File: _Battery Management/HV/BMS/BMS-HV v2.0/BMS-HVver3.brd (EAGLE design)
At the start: 152.4 x 124.8 mm, 428 parts, among them J3 M2S02B-PASK-2(LF)(SN), J4 M2S02B-PASK-2(LF)(SN), Q1 BSS308PE, Q10 BSS308PE, Q11 BSS308PE, Q12 BSS308PE, Q13 BSS308PE, Q14 BSS308PE, Q15 BSS308PE, Q16 BSS308PE, Q17 BSS308PE, Q18 BSS308PE, Q19 BSS308PE, Q2 BSS308PE, Q20 BSS308PE, Q21 BSS308PE, Q22 BSS308PE, Q23 BSS308PE, Q24 BSS308PE, Q25 BSS308PE, Q26 BSS308PE, Q27 BSS308PE, Q28 BSS308PE, Q29 BSS308PE, Q3 BSS308PE, Q30 BSS308PE, Q31 BSS308PE, Q32 BSS308PE, Q33 BSS308PE, Q34 BSS308PE, Q35 BSS308PE, Q36 BSS308PE, Q37 BSS308PE, Q38 BSS308PE, Q39 BSS308PE, Q4 BSS308PE, Q5 BSS308PE, Q6 BSS308PE, Q7 BSS308PE, Q8 BSS308PE, Q9 BSS308PE, U1 LTC6804-2, U2 LTC6804-2, U3 LTC6804-2

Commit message: BMS Redo
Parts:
- removed R54, R55, R56, R57, R58, R59, R60, R61, R62, R63, R64, R65: 16, FSAE Electric:RR02J16RTB
- R42, R43, R44, R45, R46, R47, R48, R49, R50, R51, R52, R53: value 16 -> (none); device FSAE Electric:RR02J16RTB -> adafruit:R2512
- moved R42 95.5 mm to (102.3, 31.2), turned to 0 degrees
- moved R43 86.8 mm to (102.3, 25.6)
- moved R44 84.6 mm to (102.3, 20.0), turned to 0 degrees
- moved R45 76.8 mm to (102.3, 14.4)
- moved R46 76.4 mm to (102.3, 8.79), turned to 0 degrees
- moved R52 74.4 mm to (102.3, -24.9), turned to 0 degrees
- moved R53 74.2 mm to (102.3, -30.5)
- moved R48 71.5 mm to (102.3, -2.44), turned to 0 degrees
- moved R50 70.8 mm to (102.3, -13.7), turned to 0 degrees
- moved R47 69.8 mm to (102.3, 3.17)
- moved R51 68.4 mm to (102.3, -19.3)
- moved R49 66.8 mm to (102.3, -8.05)
- moved D24 20.6 mm to (-22.0, -46.1), turned to 270 degrees
- moved D23 19.6 mm to (-22.1, -38.6), turned to 270 degrees
- moved D22 18.9 mm to (-22.1, -31.1), turned to 270 degrees
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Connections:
- net N$10: now also R44.2; no longer R60.P$2, R61.P$2
- net N$12: now also R44.1; no longer R60.P$1, R61.P$1
- net N$14: now also R45.2; no longer R58.P$2, R59.P$2
- net N$16: now also R45.1; no longer R58.P$1, R59.P$1
- net N$18: now also R46.2; no longer R56.P$2, R57.P$2
- net N$2: now also R42.2; no longer R64.P$2, R65.P$2
- net N$21: now also R48.2; no longer R52.P$2, R53.P$2
- net N$23: now also R46.1; no longer R56.P$1, R57.P$1
- net N$25: now also R47.2; no longer R54.P$2, R55.P$2
- net N$27: now also R47.1; no longer R54.P$1, R55.P$1
- net N$28: now also R48.1; no longer R52.P$1, R53.P$1
- net N$30: now also R49.2; no longer R50.P$2, R51.P$2
- net N$32: now also R49.1; no longer R50.P$1, R51.P$1
- net N$34: now also R50.2; no longer R48.P$2, R49.P$2
- net N$36: now also R50.1; no longer R48.P$1, R49.P$1
- net N$38: now also R51.2; no longer R46.P$2, R47.P$2
- net N$4: now also R42.1; no longer R64.P$1, R65.P$1
- net N$40: now also R51.1; no longer R46.P$1, R47.P$1
- net N$42: now also R52.2; no longer R44.P$2, R45.P$2
- net N$47: now also R53.2; no longer R42.P$2, R43.P$2
- net N$48: now also R53.1; no longer R42.P$1, R43.P$1
- net N$49: now also R52.1; no longer R44.P$1, R45.P$1
- net N$6: now also R43.2; no longer R62.P$2, R63.P$2
- net N$8: now also R43.1; no longer R62.P$1, R63.P$1
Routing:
- net GPIO1: track 69.8 -> 0.00 mm, vias 2 -> 0
- net GPIO2: track 61.6 -> 0.00 mm, vias 3 -> 0
- net IMA2: track 165.6 -> 105.1 mm, vias 2 -> 1
- net IPA2: track 156.5 -> 97.2 mm, vias 2 -> 1
- net IPA: track 105.3 -> 52.5 mm, vias 4 -> 3
- net IMA: track 121.9 -> 69.8 mm, vias 4 -> 3
- net N$170: track 53.3 -> 3.50 mm
- net C0: track 108.9 -> 61.3 mm, vias 1 -> 0
- net VREF2: track 40.8 -> 0.00 mm, vias 3 -> 0
- net GPIO4: track 39.9 -> 0.00 mm, vias 2 -> 0
- net VREG: track 36.8 -> 1.74 mm, vias 1 -> 0
- net GPIO3: track 31.7 -> 0.00 mm, vias 2 -> 0
- net DRIVE: track 28.8 -> 0.00 mm
- net N$103: track 3.15 -> 27.5 mm
- net A0: track 20.7 -> 0.00 mm, vias 2 -> 0
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
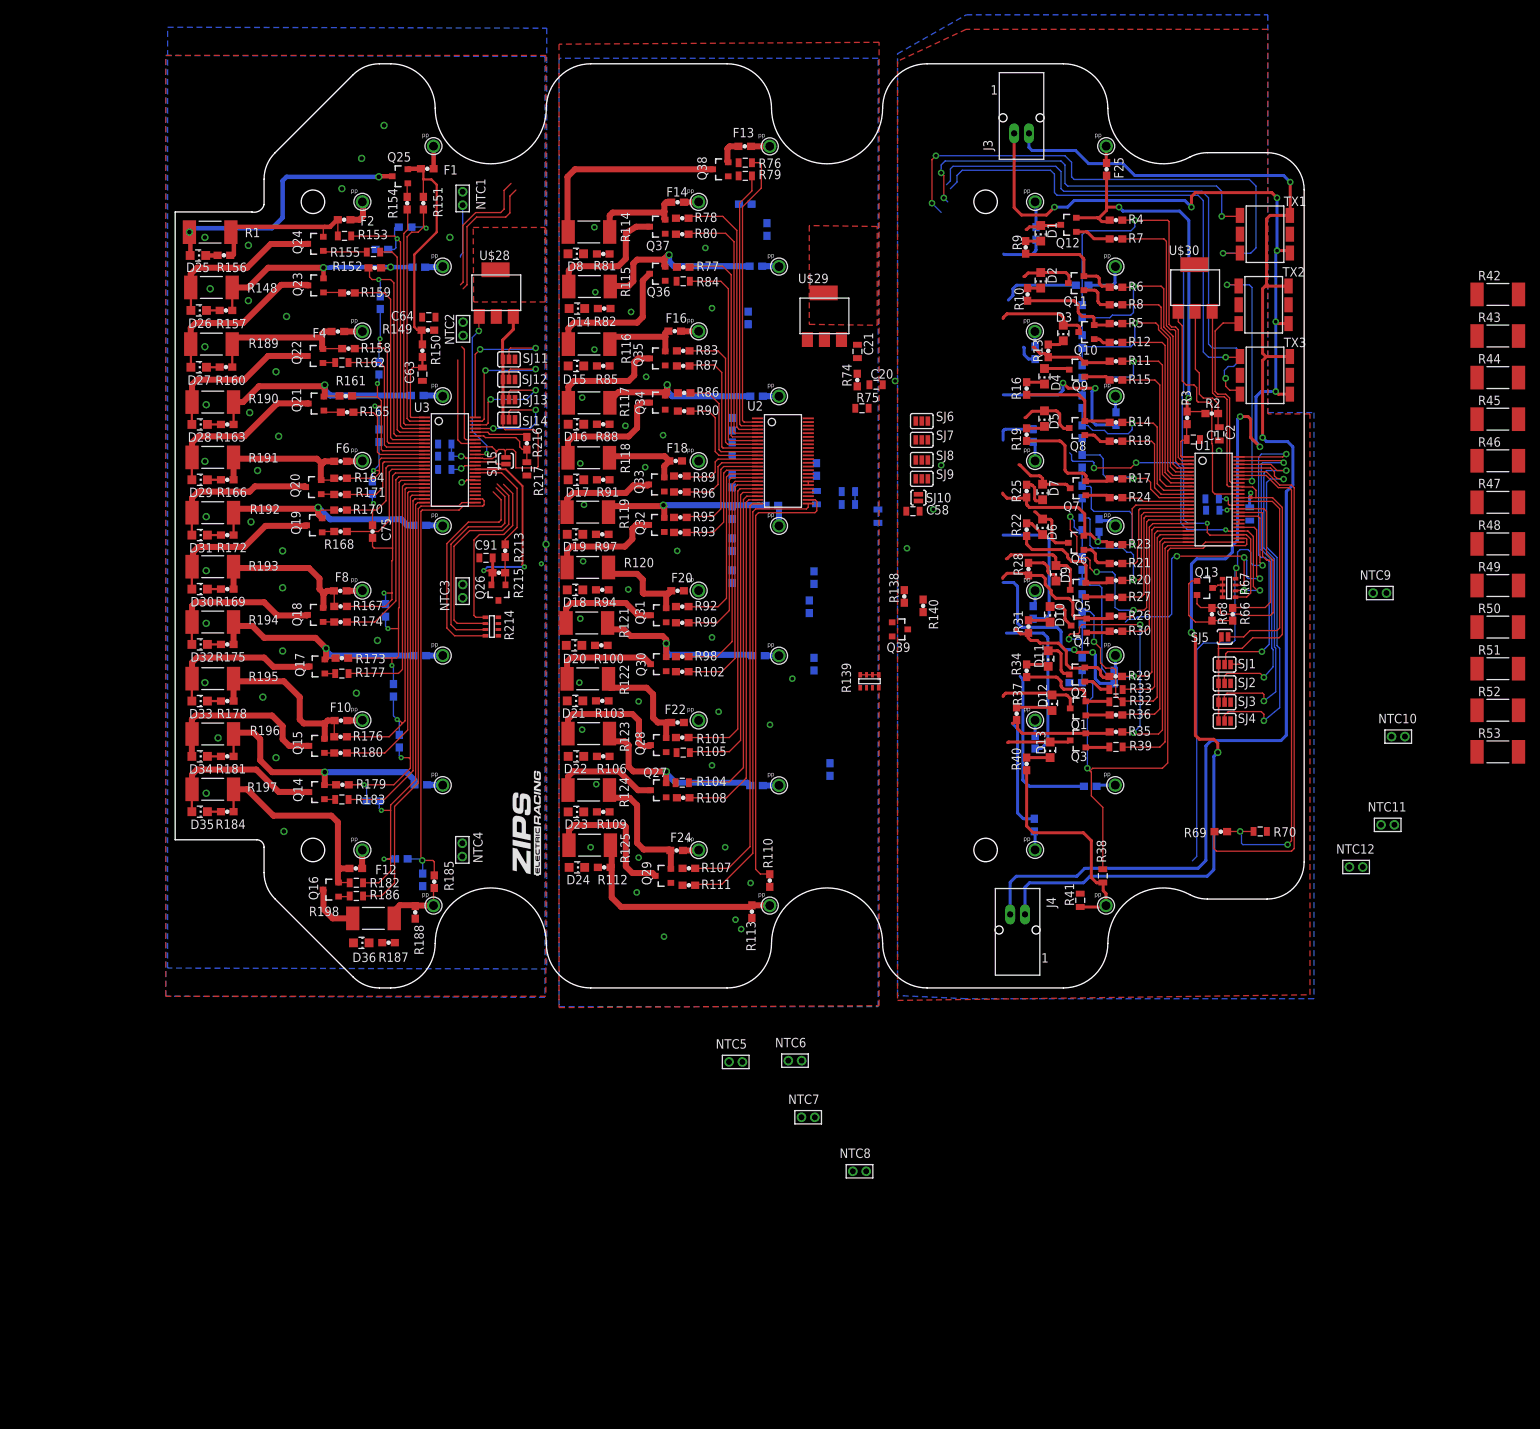
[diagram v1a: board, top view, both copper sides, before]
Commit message: 
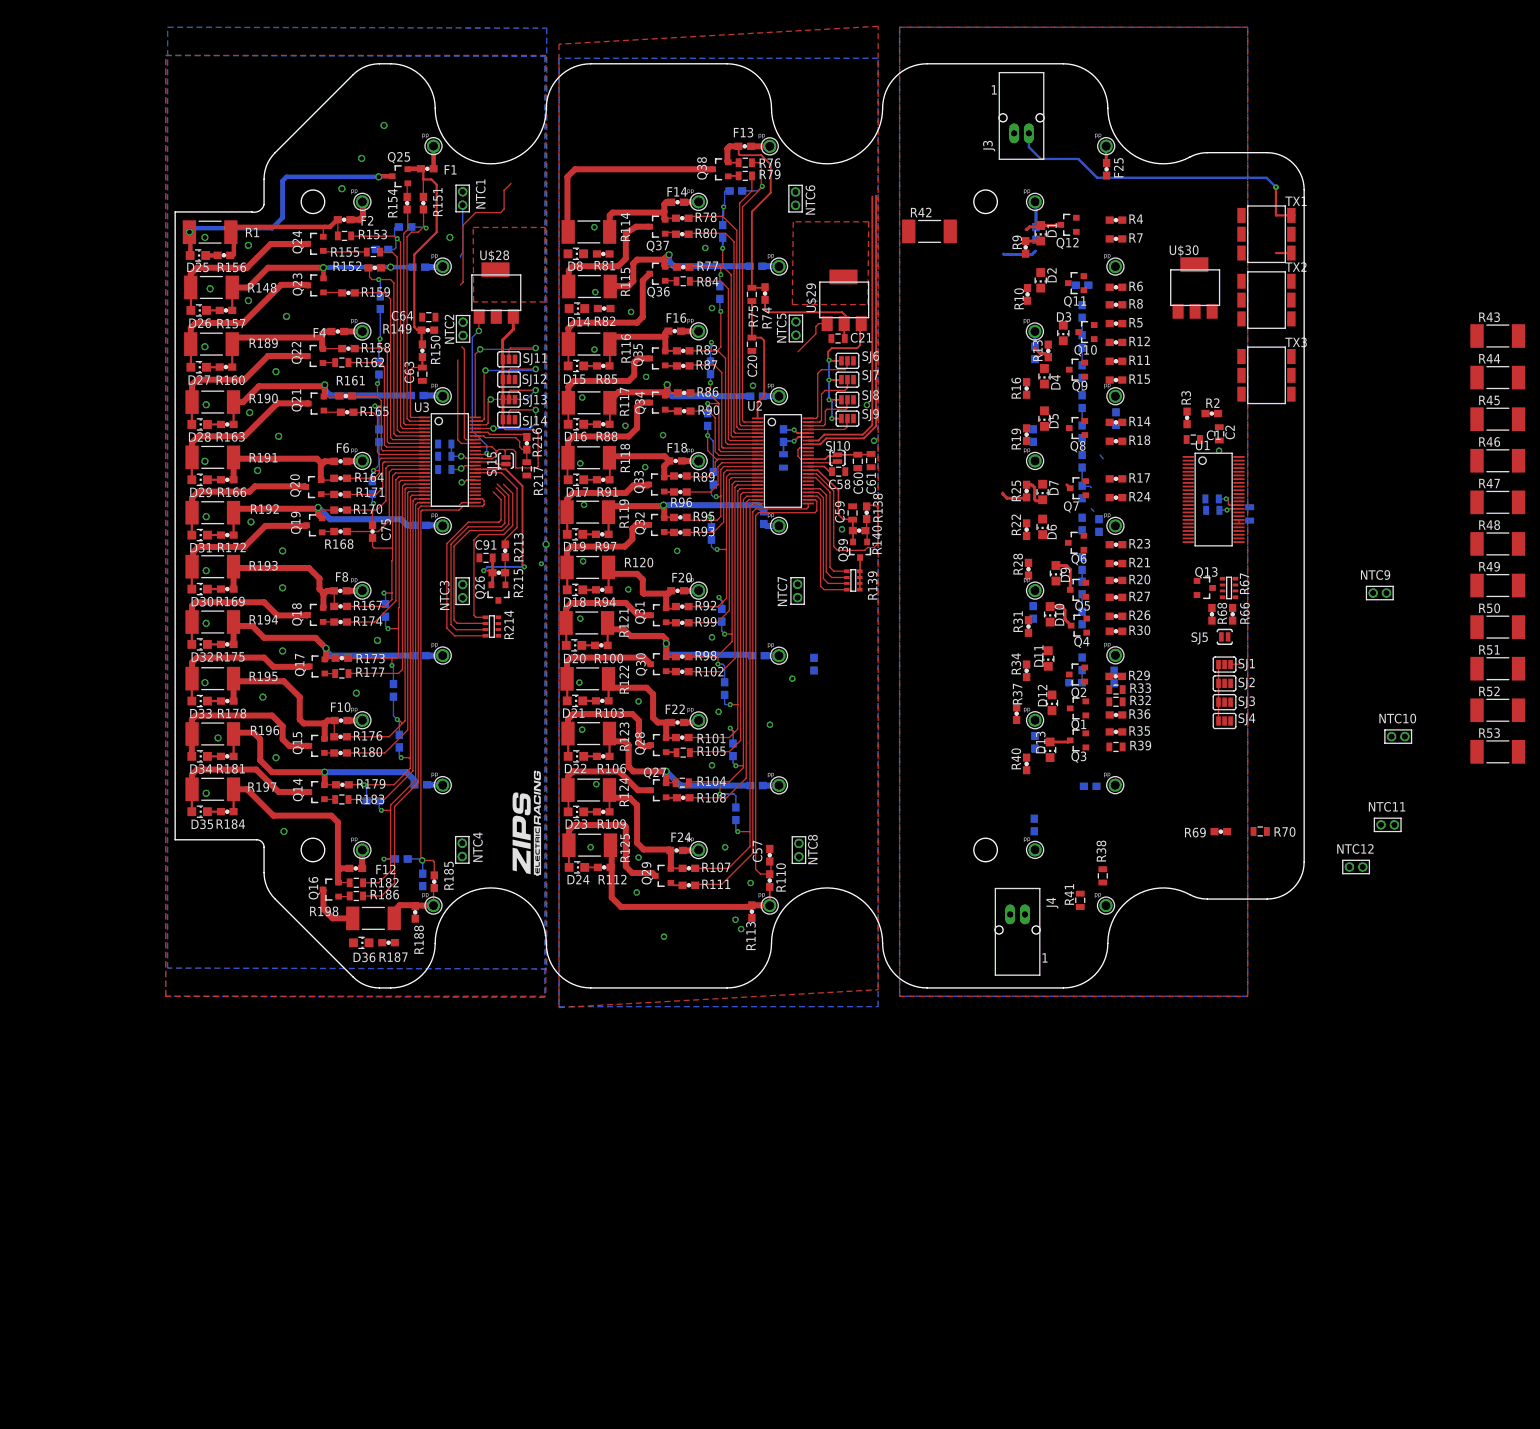
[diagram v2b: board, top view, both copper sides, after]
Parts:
- moved NTC6 116.4 mm to (7.54, 44.2), turned to 90 degrees
- moved NTC5 99.3 mm to (7.59, 26.6), turned to 90 degrees
- moved R42 77.2 mm to (25.6, 39.8)
- moved NTC7 71.1 mm to (7.82, -8.79), turned to 90 degrees
- moved NTC8 44.1 mm to (8.00, -43.8), turned to 90 degrees
- moved C53 29.6 mm to (-0.51, -38.9)
- moved C51 25.7 mm to (-0.89, -30.2)
- moved R75 21.4 mm to (1.65, 31.2), turned to 270 degrees
- moved C20 17.6 mm to (1.65, 24.5), turned to 270 degrees
- moved R74 17.1 mm to (3.43, 31.4), turned to 270 degrees
- moved C49 15.1 mm to (-2.03, -22.0)
- moved C57 14.1 mm to (4.06, -44.5), flipped to the top, turned to 90 degrees
- moved R139 13.8 mm to (15.4, -7.37), turned to 270 degrees
- moved R140 13.3 mm to (16.1, -0.64), turned to 180 degrees
- moved SJ6 12.9 mm to (14.6, 22.3)
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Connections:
- new net N$109: NTC8.2
- net GNDA: no longer NTC8.1
- net GPIO1: now also R139.4; no longer NTC5.2, R139.1
- net GPIO2: now also R139.3; no longer NTC6.2, R139.2
- net GPIO3: now also R139.2; no longer NTC7.2, R139.3
- net GPIO4: now also R139.1; no longer NTC8.2, R139.4
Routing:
- net N$129: track 195.9 -> 2.08 mm, vias 10 -> 0
- net N$125: track 186.3 -> 43.8 mm, vias 2 -> 1
- net IPA2: track 97.2 -> 14.0 mm, vias 1 -> 0
- net C23: track 82.0 -> 1.69 mm, vias 1 -> 0
- net VREG1: track 87.0 -> 7.66 mm, vias 1 -> 0
- net IMA2: track 105.1 -> 31.9 mm, vias 1 -> 0
- net IBIAS1: track 70.5 -> 0.00 mm
- net ICMP1: track 67.5 -> 0.00 mm, vias 2 -> 0
- net C21: track 66.9 -> 0.00 mm, vias 3 -> 0
- net GPIO8: track 62.7 -> 0.00 mm, vias 2 -> 0
- net C13: track 58.5 -> 0.00 mm, vias 1 -> 0
- net GPIO7: track 56.2 -> 0.00 mm, vias 1 -> 0
- net N$46: track 51.3 -> 0.00 mm, vias 2 -> 0
- net A4: track 50.7 -> 0.00 mm, vias 2 -> 0
- net A5: track 49.4 -> 0.00 mm, vias 2 -> 0
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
